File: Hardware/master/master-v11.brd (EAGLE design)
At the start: 58 x 61.2 mm, 48 parts, among them J1 22-05-7028-02

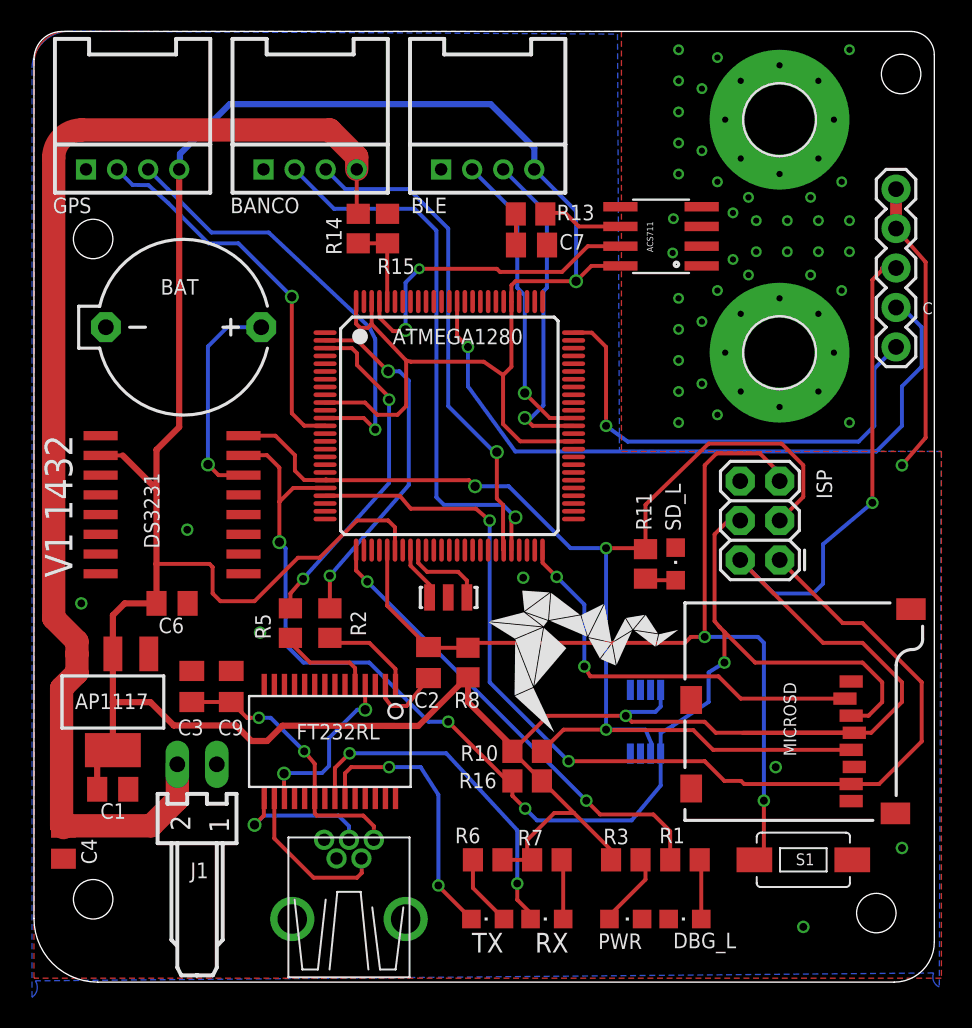
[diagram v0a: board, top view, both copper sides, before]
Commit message: BOM actualizado + cambio de R en FAULT
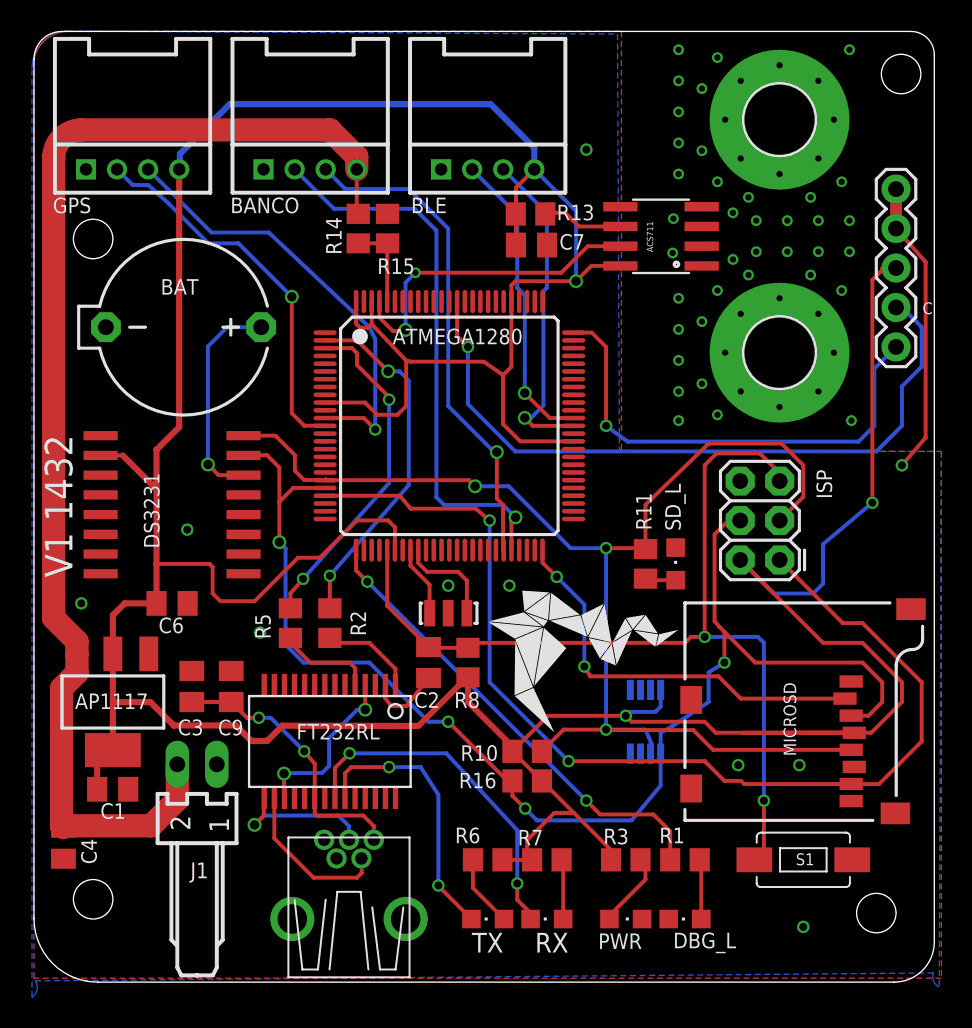
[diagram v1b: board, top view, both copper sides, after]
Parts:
- R13: value 1k -> 10k
- moved U$1 25.4 mm to (57.8, 5.08)
- moved U$2 9.67 mm to (34.9, 18.3)
- moved OSC 1.02 mm to (26.7, 23.5)
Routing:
- net 3.3V: track 286.8 -> 292.2 mm
- net N$2: track 5.52 -> 6.53 mm
- net N$14: track 3.56 -> 4.57 mm
- net GND: vias 8 -> 10

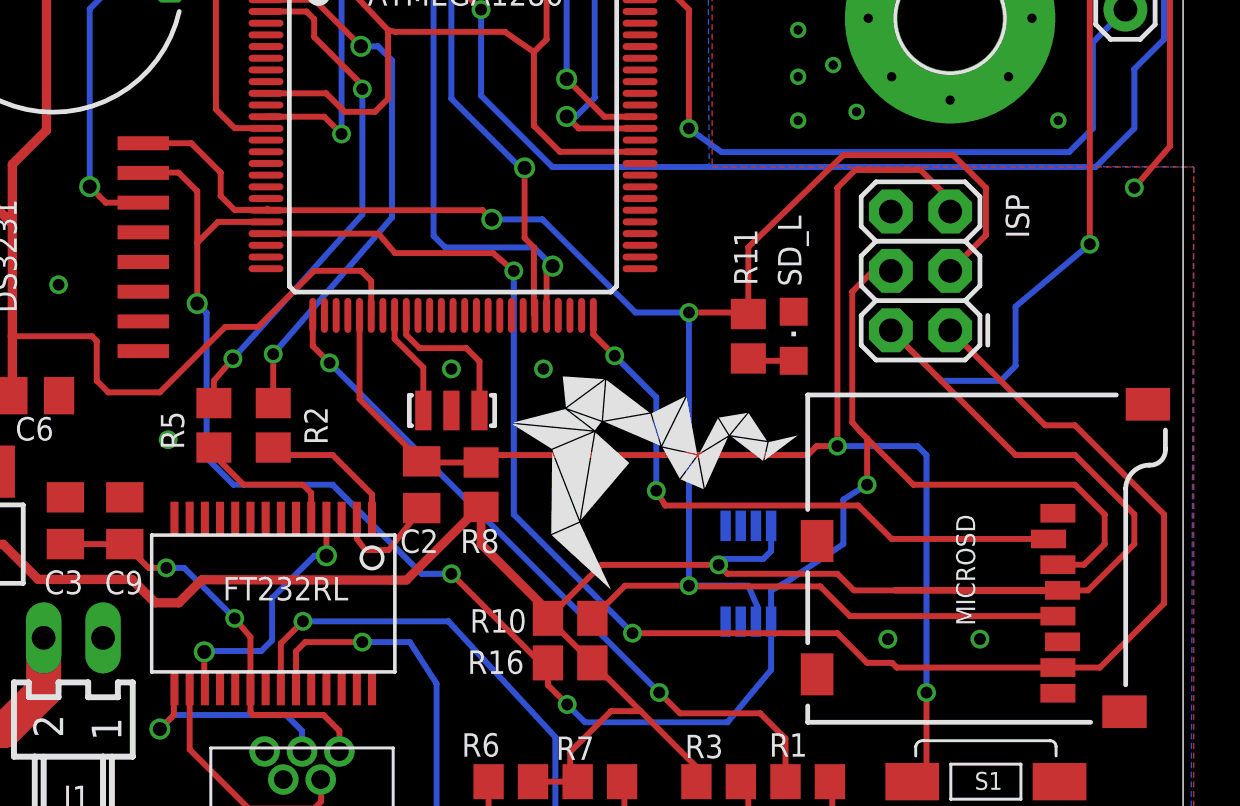
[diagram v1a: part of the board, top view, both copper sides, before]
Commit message: fix RTC and Temp wires
In schematic
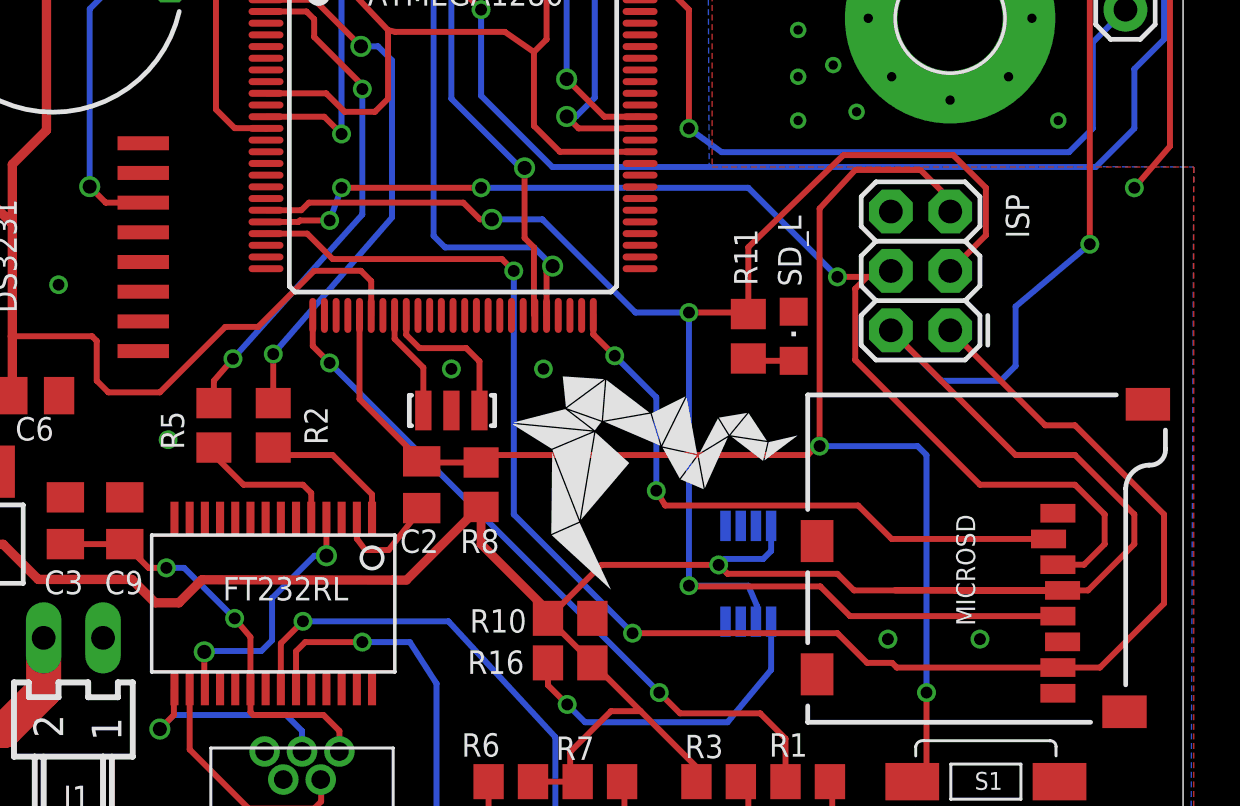
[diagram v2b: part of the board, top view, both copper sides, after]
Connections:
- new net SCL: ATMEGA1280.43, DS3231.16, R10.2, TEMP.2
- new net SDA: ATMEGA1280.44, DS3231.15, R16.2, TEMP.1
- net MOSI: no longer DS3231.15, R16.2, TEMP.1
- net SCK: no longer DS3231.16, R10.2, TEMP.2
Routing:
- net MOSI: track 84.1 -> 50.5 mm
- net SDA: track 0.00 -> 14.3 mm, vias 0 -> 1
- net SCK: track 86.4 -> 74.8 mm
